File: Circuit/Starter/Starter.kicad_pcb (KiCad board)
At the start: 2 copper layers, 259.1 x 137.2 mm, 14 parts, among them J1 From Power, J2 Output+, J3 Output-, T1 BSH12-N406L 8:6400, T2 20:20, T3 20:20

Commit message: [Circuit] Optimize circuit diagrams
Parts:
- added R4: 1Ω/10W, Resistor_THT:R_Axial_DIN0922_L20.0mm_D9.0mm_P25.40mm_Horizontal, F.Cu at (165.1, 129.5)
- moved T2 52.3 mm to (124.5, 83.8)
- moved D1 52.1 mm to (172.7, 83.8)
- moved T3 49.0 mm to (179.1, 153.7)
- moved J3 45.8 mm to (226.1, 149.9)
- moved J2 45.8 mm to (226.1, 83.8)
- moved D2 40.2 mm to (172.7, 149.9)
- moved R3 27.9 mm to (111.8, 124.5), turned to 270 degrees
- moved E1 25.4 mm to (109.2, 48.3), turned to 0 degrees
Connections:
- T2 pad 4: Net-(T2-Pad4) -> Net-(R4-Pad2)
- T3 pad 2: Net-(T2-Pad4) -> Net-(R4-Pad1)
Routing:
- net Net-(T2-Pad4): track 43.5 -> 0.00 mm
- net Net-(R4-Pad1): track 0.00 -> 27.2 mm
- net Net-(D1-Pad1): track 126.7 -> 107.8 mm
- net Net-(R4-Pad2): track 0.00 -> 18.0 mm
- net Net-(C2-Pad2): track 151.2 -> 133.7 mm
- net Net-(C1-Pad1): track 100.4 -> 87.9 mm
- net Net-(E1-Pad2): track 55.4 -> 60.4 mm
- net Net-(D2-Pad2): track 12.4 -> 7.62 mm
- net /Output-: track 12.7 -> 16.5 mm
- net Net-(D1-Pad2): track 9.84 -> 7.62 mm
- net /Output+: track 14.5 -> 16.5 mm
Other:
- board size 259.1 x 137.2 mm -> 218.4 x 137.2 mm

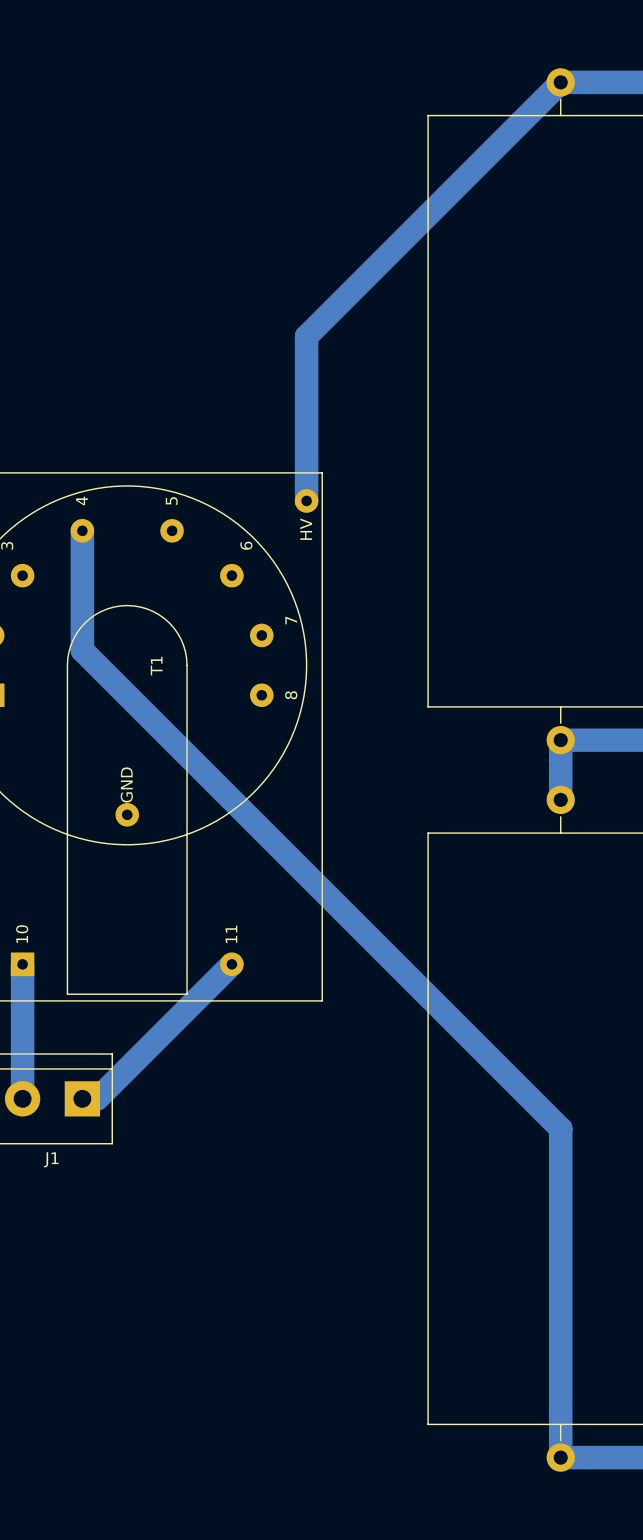
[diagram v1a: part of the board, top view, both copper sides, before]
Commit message: [Circuit] Update the turns of transformers
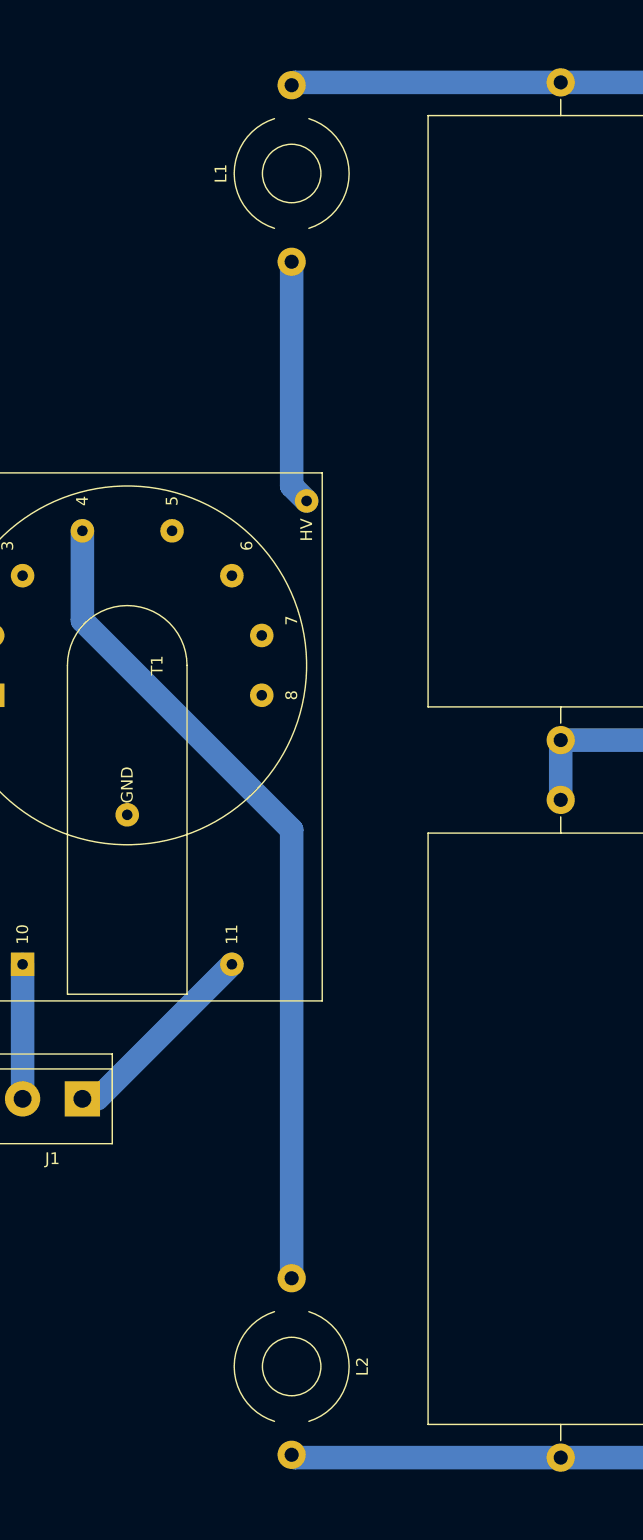
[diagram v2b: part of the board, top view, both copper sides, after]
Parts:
- added L1: 10uH, Inductor_THT:L_Toroid_Horizontal_D9.5mm_P15.00mm_Diameter10-5mm_Amidon-T37, F.Cu at (50.8, 48.3)
- added L2: 10uH, Inductor_THT:L_Toroid_Horizontal_D9.5mm_P15.00mm_Diameter10-5mm_Amidon-T37, F.Cu at (50.8, 134.6)
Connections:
- T1 pad 12: Net-(C1-Pad1) -> Net-(L1-Pad1)
- T1 pad 4: Net-(C2-Pad2) -> Net-(L2-Pad1)
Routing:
- net Net-(C2-Pad2): track 133.7 -> 61.1 mm
- net Net-(L2-Pad1): track 0.00 -> 70.9 mm
- net Net-(C1-Pad1): track 87.9 -> 66.3 mm
- net Net-(L1-Pad1): track 0.00 -> 20.8 mm

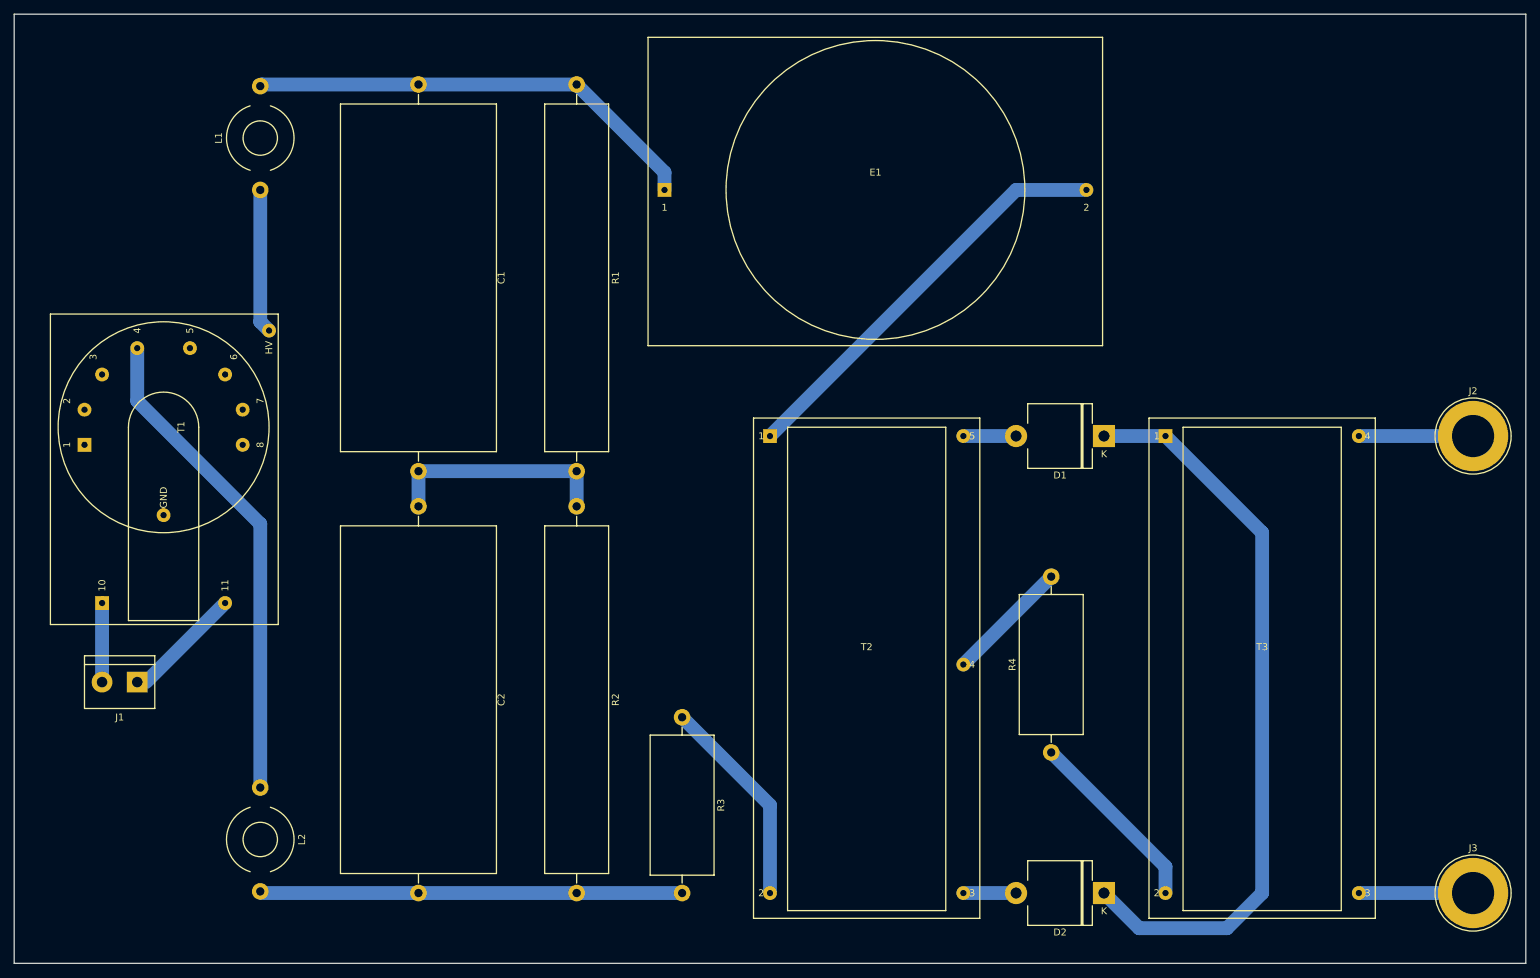
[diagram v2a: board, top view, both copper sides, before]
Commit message: [Circuit] Use full bridge rectifier instead of center tapped rectifier in starter
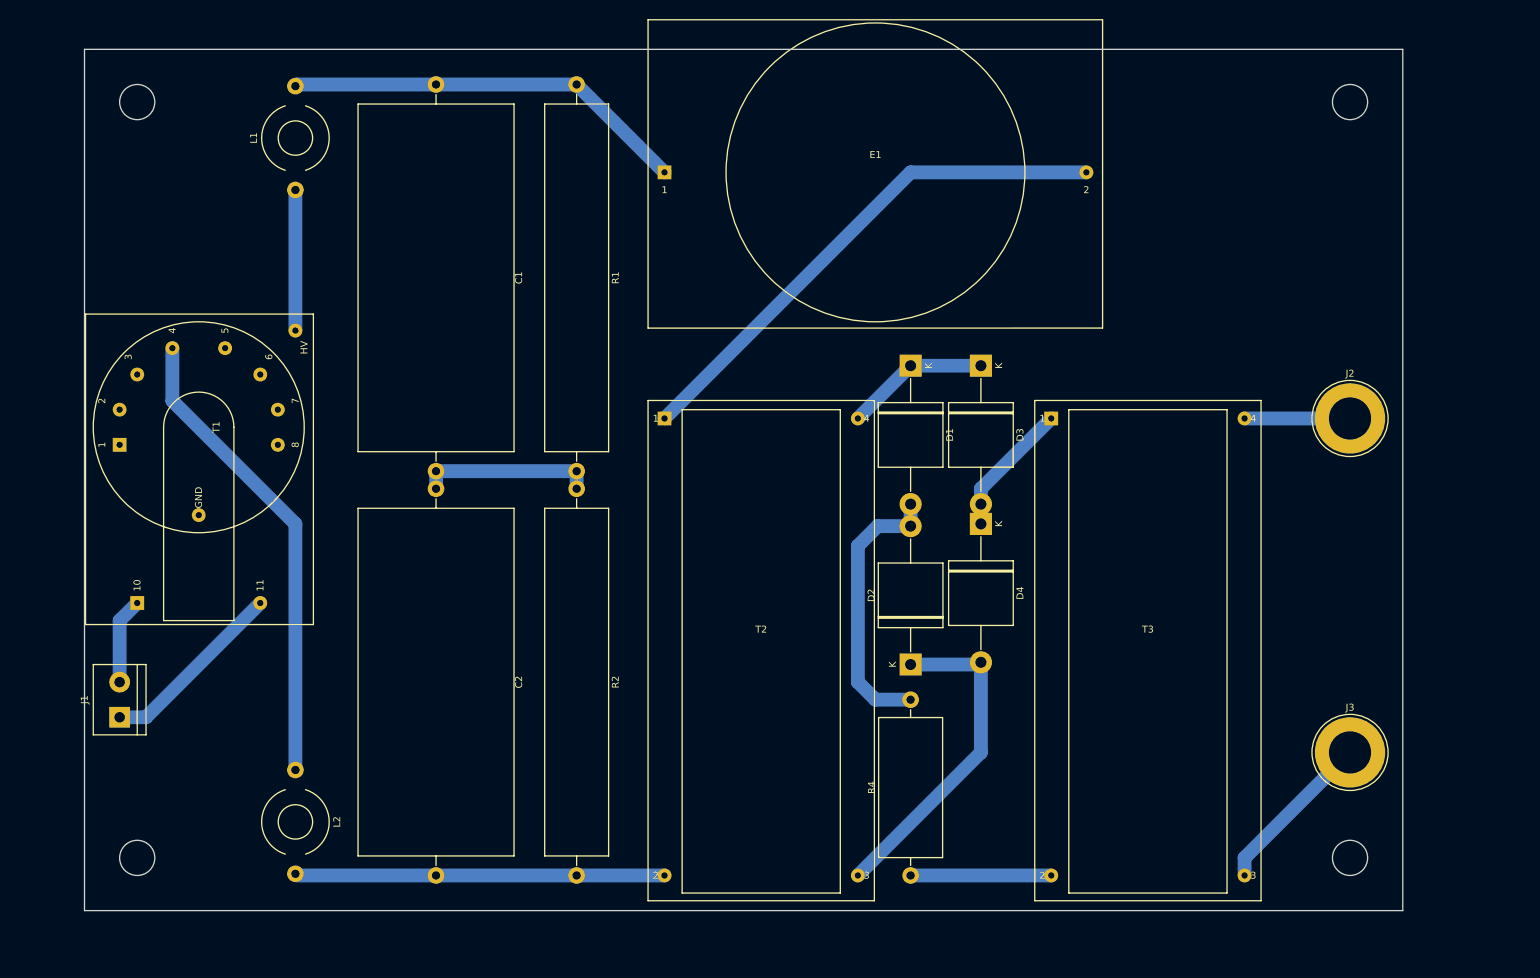
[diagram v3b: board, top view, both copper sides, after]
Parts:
- removed R3: 1Ω/10W, Resistor_THT:R_Axial_DIN0922_L20.0mm_D9.0mm_P25.40mm_Horizontal
- added D3: 2CL2FM, Diode_THT:D_P600_R-6_P20.00mm_Horizontal, F.Cu at (154.9, 73.7)
- added D4: 2CL2FM, Diode_THT:D_P600_R-6_P20.00mm_Horizontal, F.Cu at (154.9, 96.5)
- D1, D2: footprint Diode_THT:D_P600_R-6_P12.70mm_Horizontal -> Diode_THT:D_P600_R-6_P20.00mm_Horizontal
- T2: footprint Power:AirCoreTransformer_1P_SS -> Power:Air_Core_Transformer_1P_1S
- T3: footprint Power:AirCoreTransformer_1P_1S -> Power:Air_Core_Transformer_1P_1S
- moved T3 73.7 mm to (165.1, 81.3)
- moved D2 43.3 mm to (144.8, 116.8), turned to 90 degrees
- moved T1 36.9 mm to (57.1, 68.6)
- moved D1 29.7 mm to (144.8, 73.7), turned to 270 degrees
- moved J3 27.0 mm to (208.3, 129.5)
- moved R4 27.0 mm to (144.8, 147.3)
- moved J2 18.0 mm to (208.3, 81.3)
- moved T2 15.5 mm to (109.2, 81.3)
- moved L2 5.68 mm to (55.9, 132.1)
- moved J1 5.68 mm to (30.5, 124.5), turned to 90 degrees
- moved L1 5.08 mm to (55.9, 48.3)
- moved C2 3.59 mm to (76.2, 91.4)
- moved C1 2.54 mm to (76.2, 33.0)
- moved R2 2.54 mm to (96.5, 91.4)
- moved E1 2.54 mm to (109.2, 45.7)
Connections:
- D2 pad 1: Net-(D1-Pad1) -> Net-(D2-Pad1)
- D2 pad 2: Net-(D2-Pad2) -> Net-(D1-Pad2)
- R4 pad 2: Net-(R4-Pad2) -> Net-(D1-Pad2)
- T2 pad 2: Net-(R3-Pad1) -> Net-(C2-Pad2)
- T2 pad 3: Net-(D2-Pad2) -> Net-(D2-Pad1)
- T2 pad 4: Net-(R4-Pad2) -> Net-(D1-Pad1)
- T3 pad 1: Net-(D1-Pad1) -> Net-(D3-Pad2)
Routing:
- net Net-(D1-Pad1): track 107.8 -> 20.9 mm
- net Net-(D2-Pad1): track 0.00 -> 48.5 mm
- net Net-(D1-Pad2): track 7.62 -> 41.0 mm
- net Net-(R3-Pad1): track 30.7 -> 0.00 mm
- net Net-(D3-Pad2): track 0.00 -> 19.8 mm
- net Net-(R4-Pad2): track 18.0 -> 0.00 mm
- net Net-(E1-Pad2): track 60.4 -> 75.7 mm
- net /PowerIn-: track 17.4 -> 27.2 mm
- net Net-(C2-Pad2): track 61.1 -> 53.1 mm
- net Net-(C1-Pad2): track 33.0 -> 25.4 mm
- net Net-(C1-Pad1): track 66.3 -> 58.7 mm
- net Net-(D2-Pad2): track 7.62 -> 0.00 mm
- net /Output-: track 16.5 -> 24.1 mm
- net Net-(R4-Pad1): track 27.2 -> 20.3 mm
- net Net-(L2-Pad1): track 70.9 -> 68.3 mm
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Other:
- board size 218.4 x 137.2 mm -> 190.5 x 124.5 mm

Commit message: [Circuit] Optimize PCBs
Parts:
- moved T2 69.4 mm to (172.7, 53.3)
- moved D1 67.5 mm to (208.3, 50.8)
- moved D2 67.5 mm to (208.3, 94.0)
- moved D3 67.5 mm to (218.4, 50.8)
- moved D4 67.5 mm to (218.4, 73.7)
- moved R4 67.5 mm to (208.3, 124.5)
- moved T3 67.1 mm to (226.1, 53.3)
- moved J2 62.5 mm to (264.2, 53.3)
- moved J3 56.8 mm to (264.2, 119.4)
- moved C2 46.4 mm to (121.9, 99.1), turned to 180 degrees
- moved C1 41.9 mm to (66.0, 73.7), turned to 0 degrees
- moved E1 39.4 mm to (147.3, 55.9), turned to 270 degrees
- moved R1 38.1 mm to (66.0, 55.9), turned to 0 degrees
- moved R2 35.9 mm to (121.9, 116.8), turned to 180 degrees
- moved L2 20.3 mm to (55.9, 111.8)
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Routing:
- net Net-(C2-Pad2): track 53.1 -> 146.1 mm
- net Net-(C1-Pad1): track 58.7 -> 121.5 mm
- net Net-(C1-Pad2): track 25.4 -> 61.0 mm
- net Net-(L2-Pad1): track 68.3 -> 50.5 mm
- net Net-(L1-Pad1): track 20.3 -> 5.08 mm
- net /Output-: track 24.1 -> 10.2 mm
- net /Output+: track 16.5 -> 10.2 mm
- net Net-(D2-Pad1): track 48.5 -> 43.4 mm
- net Net-(D3-Pad2): track 19.8 -> 23.8 mm
- net Net-(D1-Pad1): track 20.9 -> 18.8 mm
- net Net-(E1-Pad2): track 75.7 -> 74.0 mm
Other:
- board size 190.5 x 124.5 mm -> 246.4 x 86.4 mm
